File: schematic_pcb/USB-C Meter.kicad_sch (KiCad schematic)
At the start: 68 parts, among them J1 USB-C Receptacle 16P, J2 USB-C Receptacle 16P, J3 Generic IN, J4 Generic OUT, J5 USB_B_Micro, J6 Display I2C, J7 Conn_Coaxial, U1 MP4560DN, U2 ME6211C33, U3 TPS2115, U4 ESP32-C3FH4, U6 INA228, Y1 40MHz

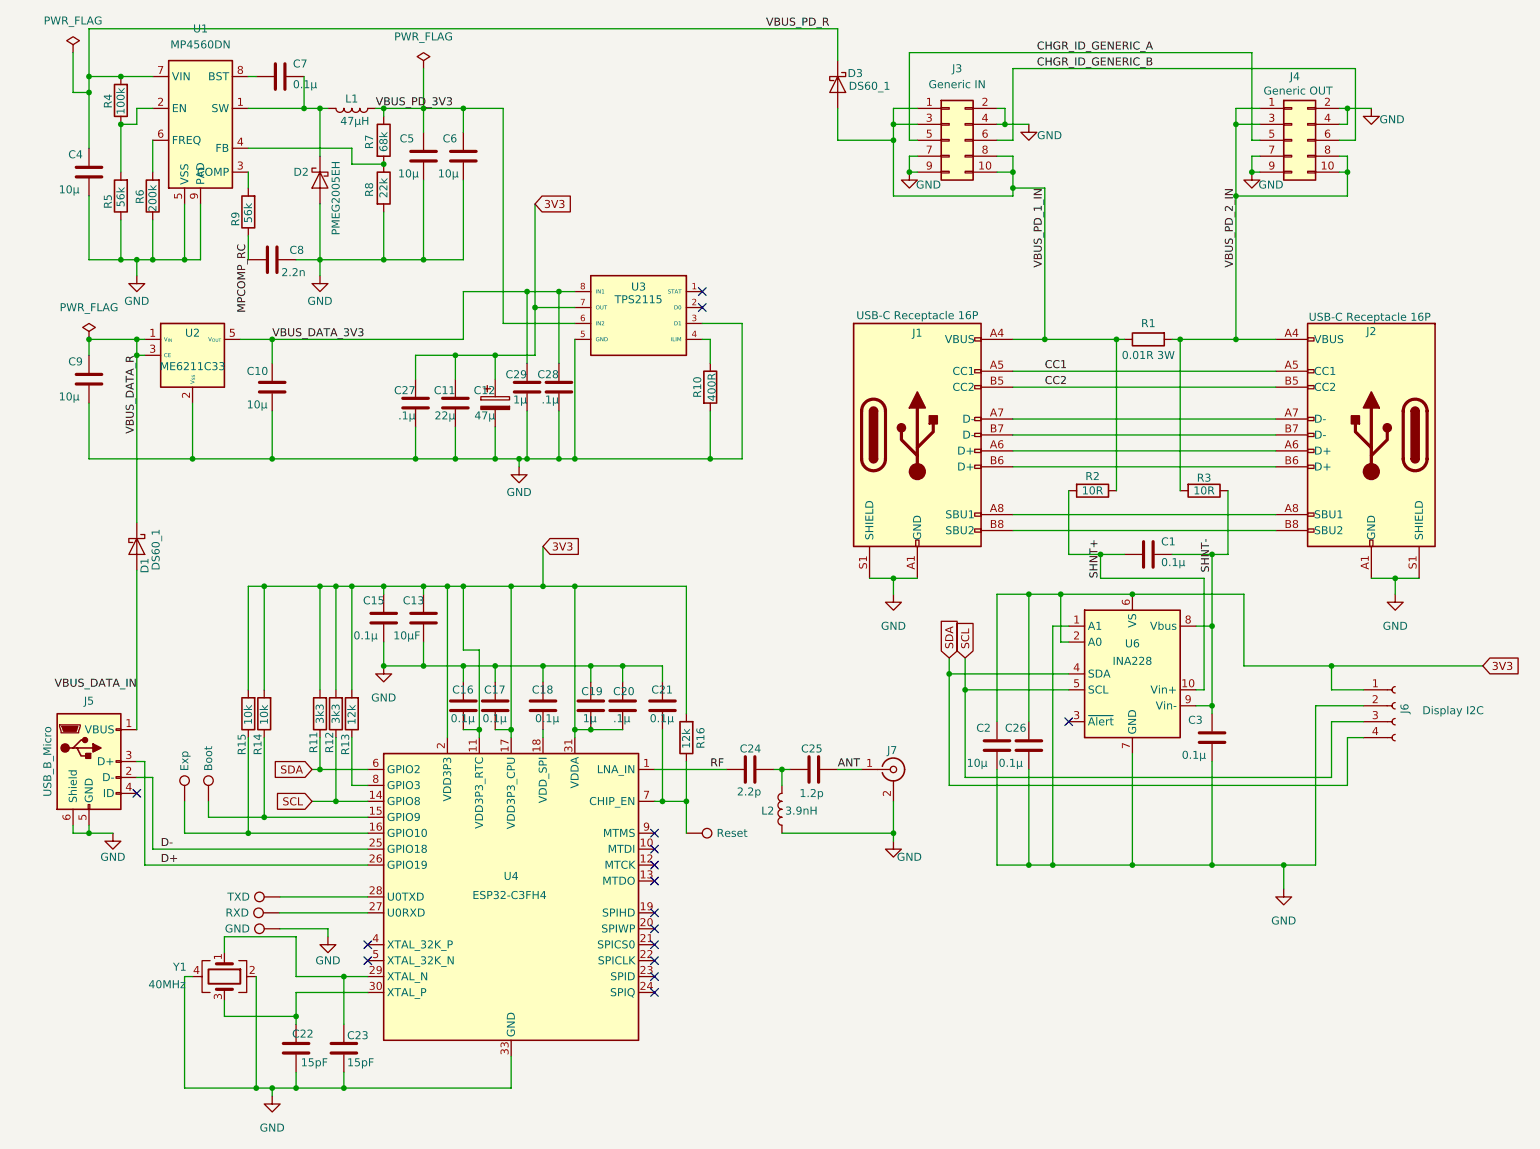
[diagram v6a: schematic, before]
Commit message: fix: rf antenna pcb design, added reset tactile switch
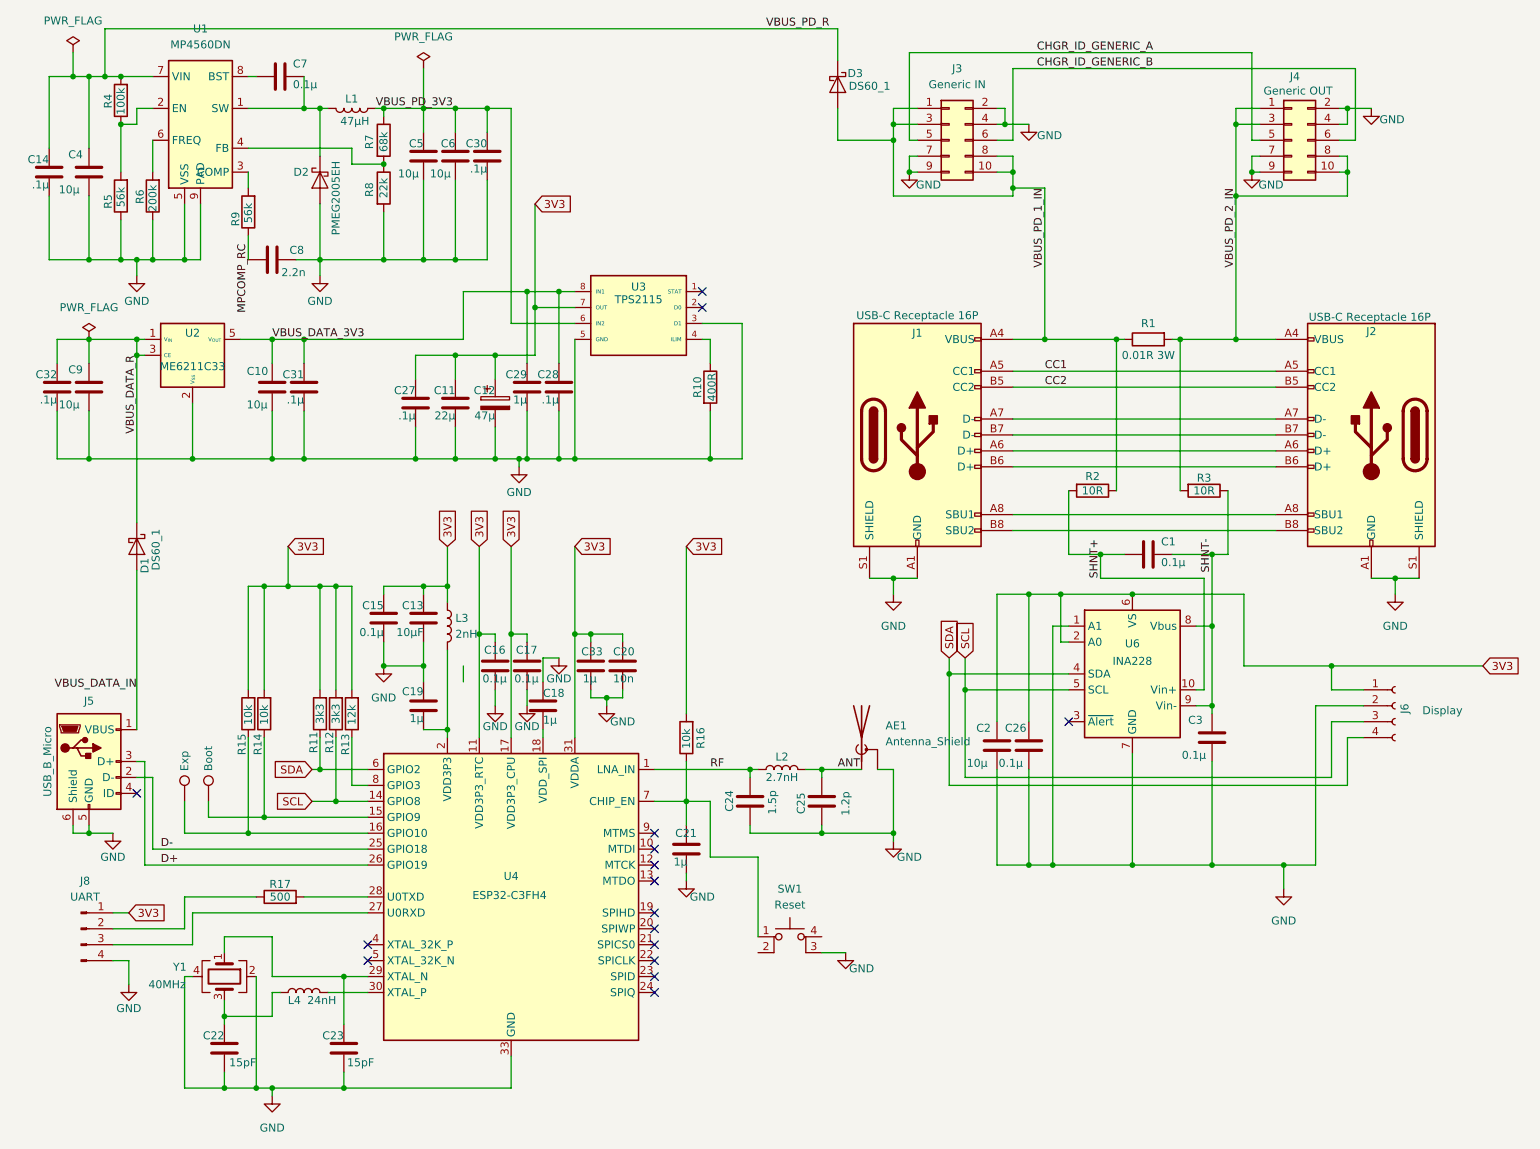
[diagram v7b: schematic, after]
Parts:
- removed J7: Conn_Coaxial, Connector_Coaxial:U.FL_Hirose_U.FL-R-SMT-1_Vertical, symbol Connector:Conn_Coaxial
- removed TP3: Reset, TestPoint:TestPoint_Pad_D1.5mm, symbol Connector:TestPoint
- removed TP4: TXD, TestPoint:TestPoint_Pad_D1.5mm, symbol Connector:TestPoint
- removed TP5: RXD, TestPoint:TestPoint_Pad_D1.5mm, symbol Connector:TestPoint
- removed TP6: GND, TestPoint:TestPoint_Pad_D1.5mm, symbol Connector:TestPoint
- added AE1: Antenna_Shield, schematic_pcb:ESPRESSIF_ESP32_MIFA_2.4GHz_Right, symbol Device:Antenna_Shield
- added C14, C30, C31, C32: .1µ, Capacitor_SMD:C_0603_1608Metric, symbol Device:C
- added C33: 1µ, Capacitor_SMD:C_0603_1608Metric, symbol Device:C
- added J8: UART, Connector_JST:JST_PH_B4B-PH-K_1x04_P2.00mm_Vertical, symbol Connector:Conn_01x04_Pin
- added L3: 2nH, Inductor_SMD:L_0201_0603Metric_Pad0.64x0.40mm_HandSolder, symbol Device:L
- added L4: 24nH, Inductor_SMD:L_0603_1608Metric_Pad1.05x0.95mm_HandSolder, symbol Device:L
- added R17: 500, Resistor_SMD:R_0603_1608Metric, symbol Device:R
- added SW1: Reset, Project:PTS647SK70SMTR2LFS, symbol Switch:SW_MEC_5E
- C18, C21: value 0.1µ -> 1µ
- C20: value .1µ -> 10n
- C24: value 2.2p -> 1.5p
- J6: value Display I2C -> Display
- L2: value 3.9nH -> 2.7nH
- R10: footprint Resistor_SMD:R_0402_1005Metric -> Resistor_SMD:R_0603_1608Metric
- R16: value 12k -> 10k
- U1: footprint Package_SO:SOIC-8_3.9x4.9mm_P1.27mm -> Package_SO:SOIC-8-1EP_3.9x4.9mm_P1.27mm_EP2.62x3.51mm_ThermalVias
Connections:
- net 3V3: now also C16.1, C17.1, C20.1, C33.1, J8.1 (Pin_1), L3.1; no longer C16.2, C17.2, C19.2, C20.2, U4.2 (VDD3P3), U4.3 (VDD3P3)
- net ANT: now also L2.2, AE1.1 (A)
- net GND: now also C16.2, C17.2, C20.2, C21.2, C24.1, C25.2, AE1.2 (Shield), C14.2, C30.2, C31.2, C32.2, C33.2, J8.4 (Pin_4), SW1.3 (K); no longer C16.1, C17.1, C20.1, C21.1, L2.1
- net RF: now also C24.2, L2.1; no longer C24.1
- net VBUS_DATA_3V3: now also C31.1
- net VBUS_DATA_R: now also C32.1
- net VBUS_PD_3V3: now also C30.1
- net VBUS_PD_R: now also C14.1
- net at R16.1, U4.7 (CHIP_EN): now also C21.1, SW1.1; no longer C21.2
- net at U4.28 (U0TXD): now also R17.2
- net at U4.27 (U0RXD): now also J8.3 (Pin_3)
- net at C22.2, Y1.3: now also L4.1; no longer U4.30 (XTAL_P)
- new net: C19.2, L3.2, U4.2 (VDD3P3), U4.3 (VDD3P3)
- new net: J8.2 (Pin_2), R17.1
- new net: L4.2, U4.30 (XTAL_P)
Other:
- moved on the sheet: C16, C17, C19, C20, C21, C22, C24, C25, C6, C9, L2

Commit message: feat: reroute antenna and all other components
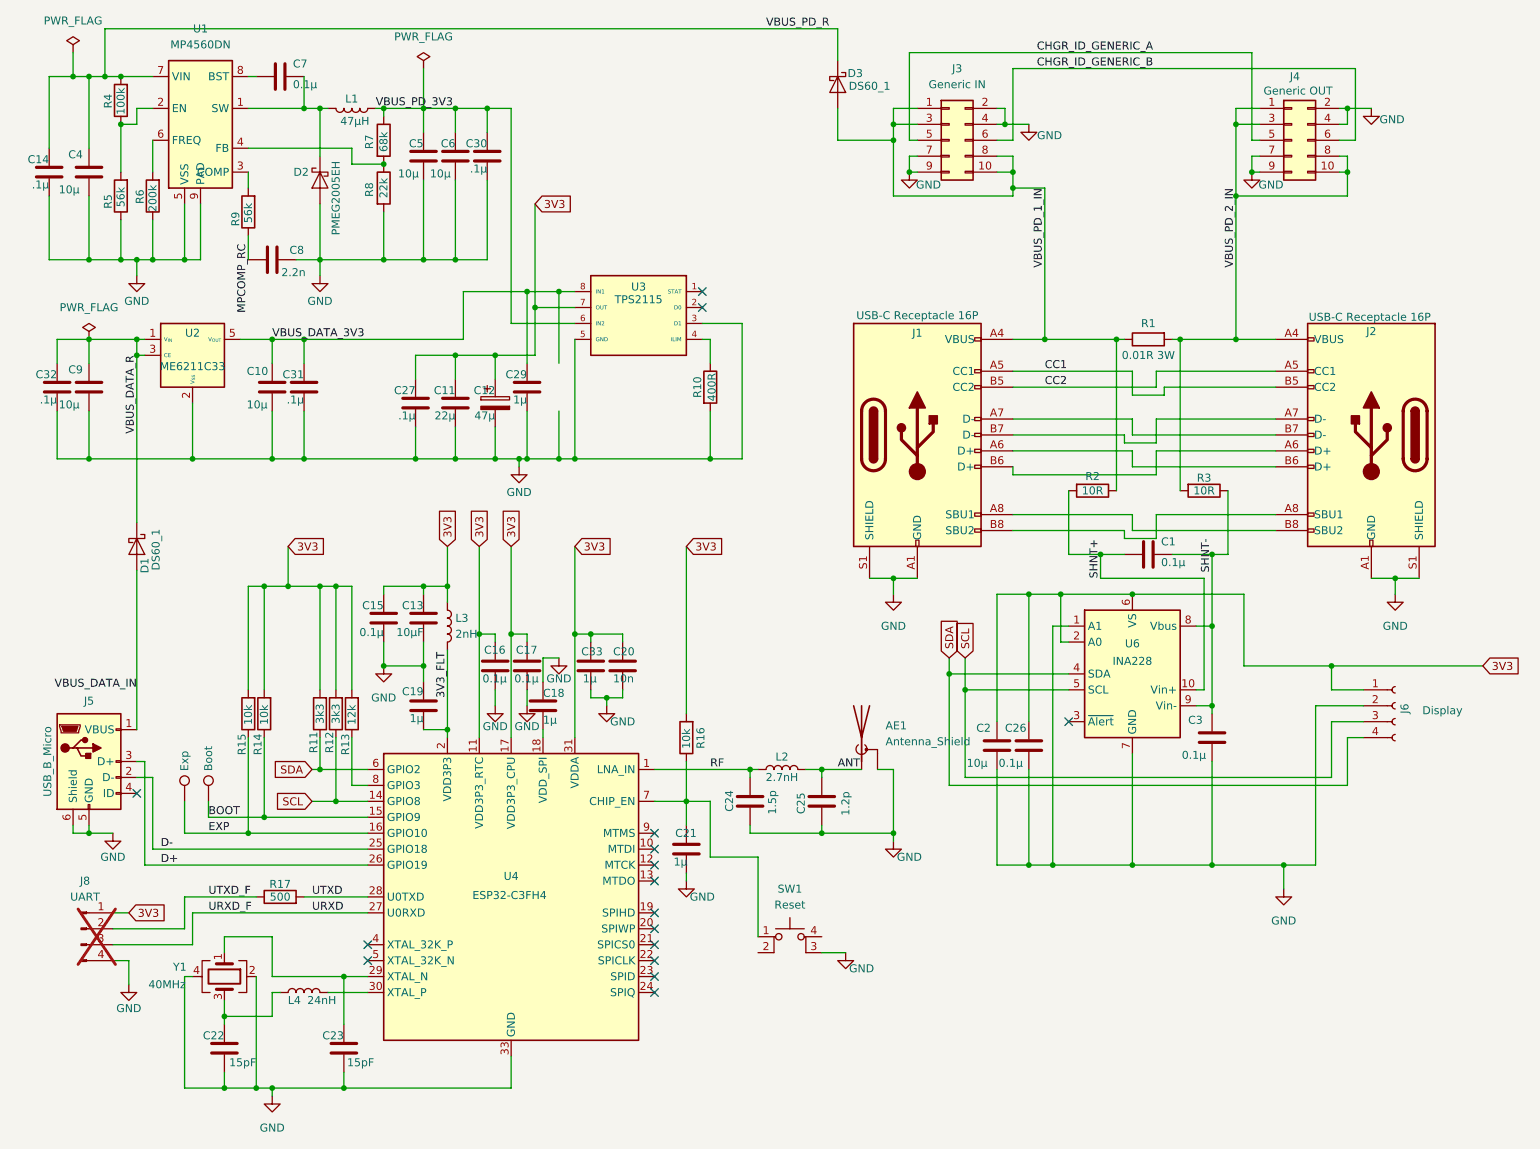
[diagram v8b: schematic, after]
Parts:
- removed C28: .1µ, Capacitor_SMD:C_0603_1608Metric, symbol Device:C
- AE1: now left out of the parts list
- C4: footprint Capacitor_SMD:C_0805_2012Metric_Pad1.18x1.45mm_HandSolder -> Capacitor_SMD:C_0603_1608Metric
- J8: now not fitted
- L3: footprint Inductor_SMD:L_0201_0603Metric_Pad0.64x0.40mm_HandSolder -> Inductor_SMD:L_0603_1608Metric; Source (none) -> https://www.digikey.de/de/products/detail/te-connectivity-p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
- L4: footprint Inductor_SMD:L_0603_1608Metric_Pad1.05x0.95mm_HandSolder -> Inductor_SMD:L_0402_1005Metric
- R11, R12, R13, R14, R15, R16, R2, R3, R4, R5, R6, R7, R8, R9: footprint Resistor_SMD:R_0603_1608Metric_Pad0.98x0.95mm_HandSolder -> Resistor_SMD:R_0603_1608Metric
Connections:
- net CC1: now also J2.B5 (CC2); no longer J2.A5 (CC1)
- net CC2: now also J2.A5 (CC1); no longer J2.B5 (CC2)
- net BOOT: now reaches R14.1, TP1.1, U4.15 (GPIO9)
- net 3V3_FLT: now reaches C19.2, L3.2, U4.2 (VDD3P3), U4.3 (VDD3P3)
- net at J2.A6 (D+): now also J1.B6 (D+); no longer J1.A6 (D+)
- net at J2.A7 (D-): now also J1.B7 (D-); no longer J1.A7 (D-)
- net at J2.A8 (SBU1): now also J1.B8 (SBU2); no longer J1.A8 (SBU1)
- net at J2.B6 (D+): now also J1.A6 (D+); no longer J1.B6 (D+)
- net at J2.B7 (D-): now also J1.A7 (D-); no longer J1.B7 (D-)
- net at J2.B8 (SBU2): now also J1.A8 (SBU1); no longer J1.B8 (SBU2)
- net UTXD_F: now reaches J8.2 (Pin_2), R17.1
- net UTXD: now reaches R17.2, U4.28 (U0TXD)
- net EXP: now reaches R15.1, TP2.1, U4.16 (GPIO10)
- net URXD: now reaches J8.3 (Pin_3), U4.27 (U0RXD)
